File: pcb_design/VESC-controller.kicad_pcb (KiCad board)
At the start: 4 copper layers, 160 x 90 mm, 304 parts, among them J1 GATE_DRIVER_CONN_U, J2 GATE_DRIVER_CONN_V, J3 GATE_DRIVER_CONN_W, J4 micro USB, J5 ACCEL, J6 REGEN, J7 12V, J8 V_BUS, J9 SWD, P1 HALL/Encoder, P101 CANBUS, P2 Resolver, P3 PWR_COMM, Q1 BSC340N08, Q2 2N7002PW, Q3 AO4805, U1 STM32F40X_LQFP64, U10 LM2903-SO8, U11 LM3488, U12 OPA2376AID, U13 LM1117IMP-v.v, U14 OPA2376AID, U15 AD2S1205, U16 OPA2376AID, U17 LM2903-SO8, U18 AND3, U19 AD8397, U2 ISO1050, U20 APX809, U21 NCV78Mxx, U3 OPA2376AID, U4 LM2903-SO8, U5 7400-TSSOP, U6 SN74ALVC08PWR, U7 SN74ALVC08PWR, U8 SN74AUP1G74, U9 LM22676QTJ-5.0, X1 ABM3B - 8MHz, X2 ABM3B - 8MHz

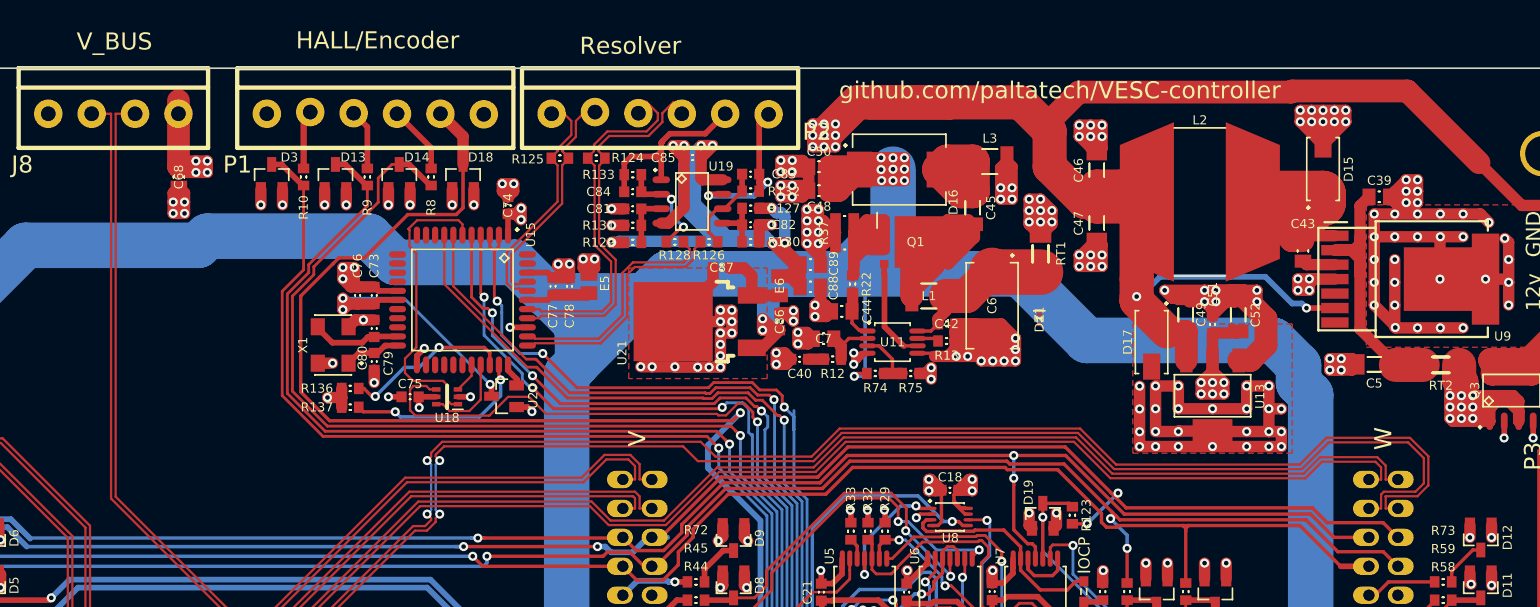
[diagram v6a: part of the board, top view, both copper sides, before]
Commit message: Had a missing pullup for the fault signal. Added silkcreens on the bottom
Signed-off-by: Marcos Chaparro <mchaparro@paltatech.com>
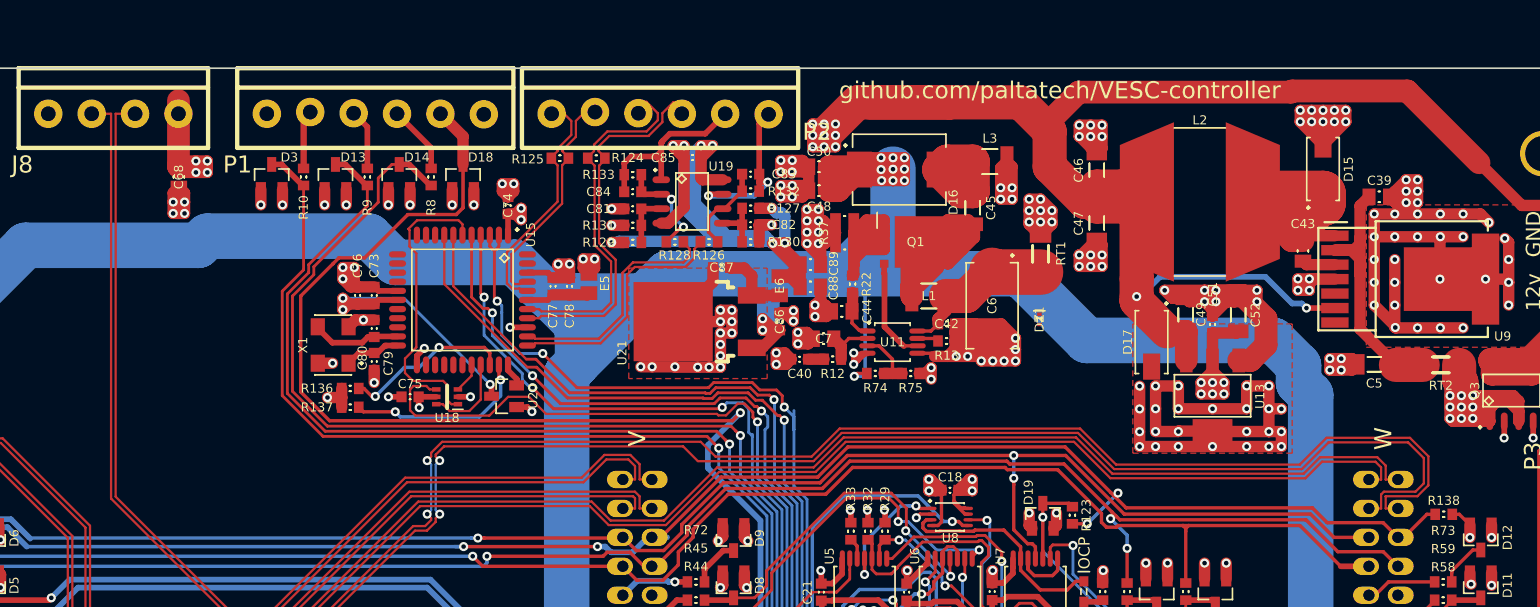
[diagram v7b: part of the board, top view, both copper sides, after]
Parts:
- added R138: 10k, IPC7351-Nominal:RESC1608X50, F.Cu at (63.8, -5.83)
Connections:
- net /MISO_RX_SCL renamed /STM32F4/MISO_ADC_EXT2
- net /RX_SCL_MOSI renamed /STM32F4/TX_SCL_MOSI
- net /SCK_ADC_EXT renamed /STM32F4/SCK_ADC_EXT
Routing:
- net ~FAULT: track 147.1 -> 151.2 mm
- net +3.3: track 192.5 -> 194.4 mm
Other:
- board text added: "+24v"
- board text added: "-VEE_CTRL"
- board text added: "3.3v"
- board text added: "5v"
- board text added: "9v-30v Supply"
- board text added: "ACCEL_IN"
- board text added: "ADC4/DAC1/RX PWM/I2C_SDA"
- board text added: "ADC5/DAC2 PWM/SPI1_SCK"
- board text added: "ADC6/PWM/ SPI1_MISO"
- board text added: "ADC7/TX PWM/I2C_SCL"
- board text added: "COS+"
- board text added: "COS-"
- board text added: "EXC+"
- board text added: "EXC-"
- board text added: "HALL_1"
- board text added: "HALL_2"
- board text added: "HALL_3"
- board text added: "I_phase+"
- board text added: "I_phase-"
- board text added: "PWM_BOT"
- board text added: "PWM_TOP"
- board text added: "PWR_GOOD"
- board text added: "REGEN_IN"
- board text added: "SIN+"
- board text added: "SIN-"
- board text added: "SUPPLY_SYNC"
- board text added: "TEMP"
- board text added: "VBUS(+)"
- board text added: "VBUS(-)"
- board text added: "V_phase+"
- board text added: "V_phase-"
- board text added: "~DRIVER_RESET"
- board text added: "~FAULT"

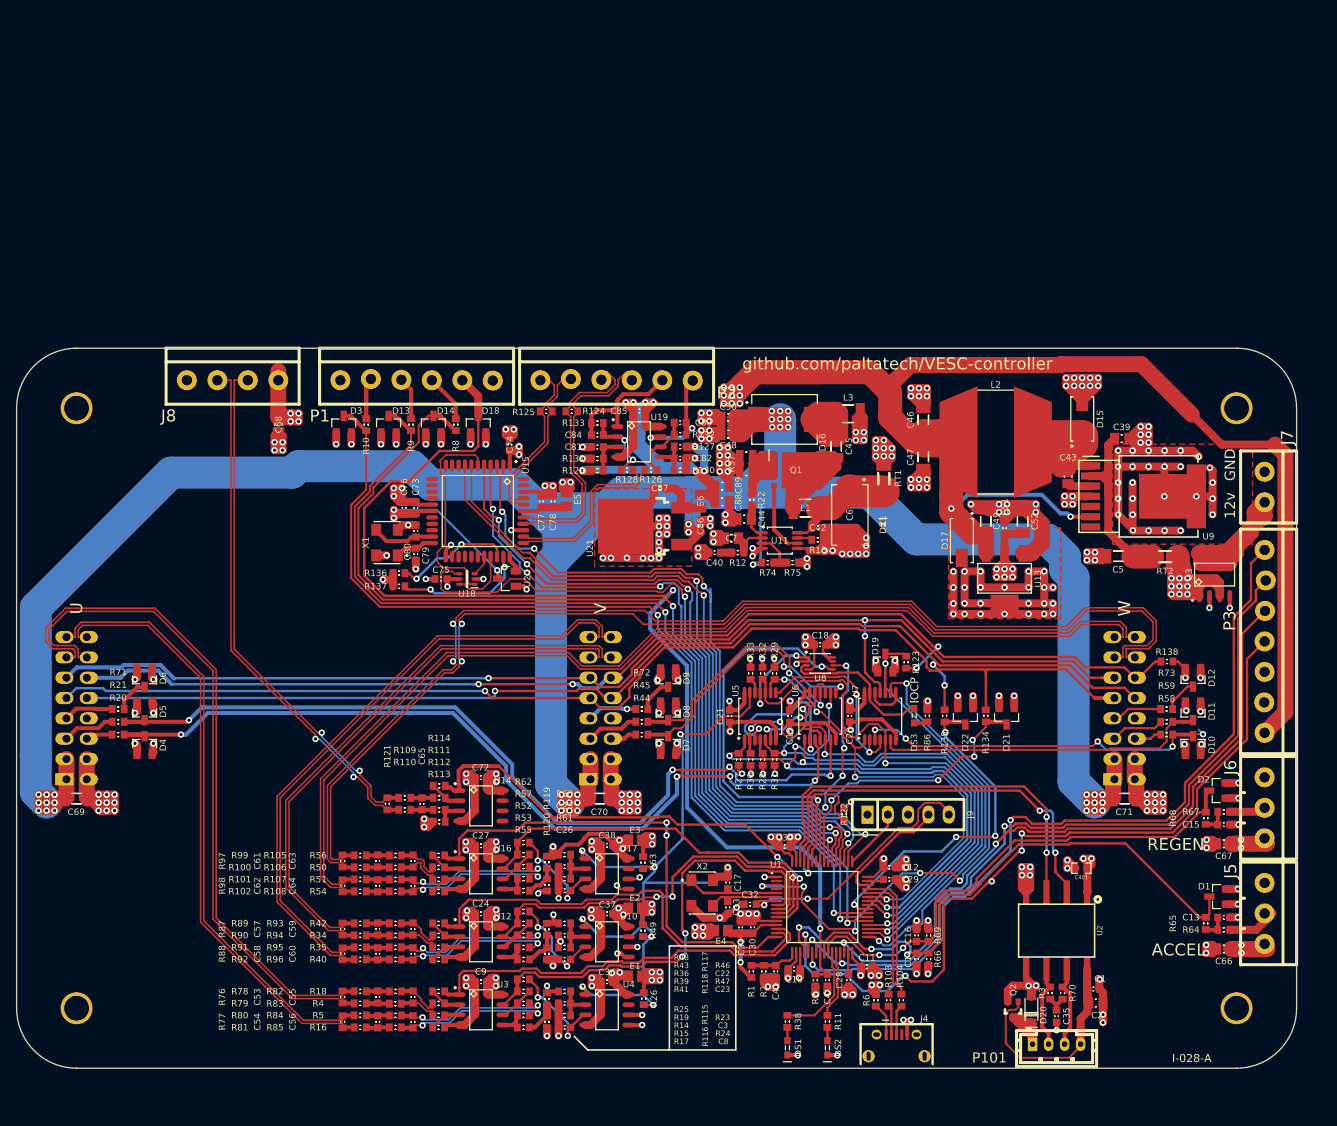
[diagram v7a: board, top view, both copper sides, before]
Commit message: Silkscreen logos, fixed swapped OCP inputs, added a button to enter bootloader,missing 3d model.
Signed-off-by: Marcos Chaparro <mchaparro@paltatech.com>
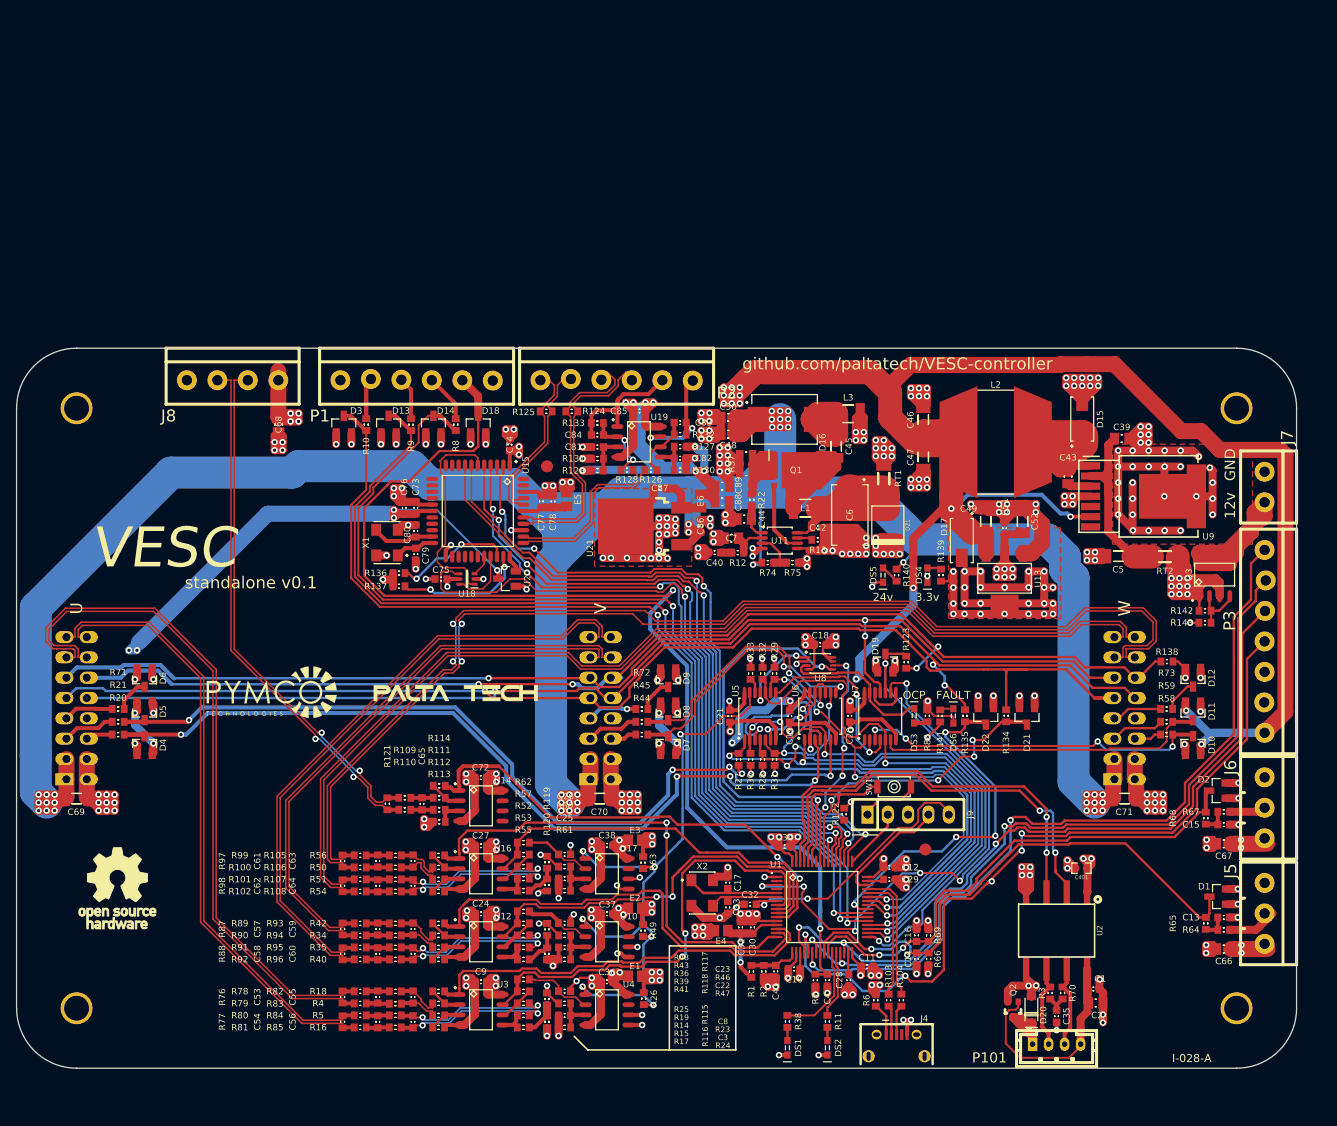
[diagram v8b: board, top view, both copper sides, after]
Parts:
- added DS4: GREEN, smd-semi:LED-0603, F.Cu at (33.8, -16.6)
- added DS5: RED, smd-semi:LED-0603, F.Cu at (28.3, -16.6)
- added DS6: FAULT, smd-semi:LED-0603, F.Cu at (37.1, 0.97)
- added G***: LOGO, paltatech:PYMCO_logo_22x15mm, F.Cu at (-48.2, -1.48)
- added G***: LOGO, mech:OSHW-10mm, F.Cu at (-67.4, 22.5)
- added G***: LOGO, paltatech:PALTA_TECH_SILKS_20mm, F.Cu at (-25.3, -1.88)
- added R139: 1k, IPC7351-Nominal:RESC1608X50, F.Cu at (35.5, -16.6)
- added R140: 10k, IPC7351-Nominal:RESC1608X50, F.Cu at (30.0, -16.6)
- added R141: 100R, IPC7351-Nominal:RESC1608X50, F.Cu at (35.4, 0.97)
- added R142: 10k, IPC7351-Nominal:RESC1608X50, F.Cu at (68.5, -12.2)
- added R143: 10k, IPC7351-Nominal:RESC1608X50, F.Cu at (68.5, -10.7)
- added REF**: FIDUCIAL-1.5mm, fab:FIDUCIAL-1.5mm, F.Cu at (-13.7, -30.2)
- added REF**: FIDUCIAL-1.5mm, fab:FIDUCIAL-1.5mm, F.Cu at (33.6, 17.7)
- added SW1: BOOTLOADER, paltatech:SMD-Switch_B3U-1000-B, F.Cu at (29.7, 9.82)
- DZ1: value ESD9L5.0ST5G -> 1SMB18CAT; footprint smd-semi:SOD-THAT -> w_smd_diode:do214aa
- U6, U7: value SN74ALVC08PWR -> SN74ACT08PWR
- moved C26 4.53 mm to (-11.5, 18.3), turned to 0 degrees
- moved C23 4.53 mm to (-11.5, 26.9), turned to 0 degrees
- moved C8 4.53 mm to (-11.5, 35.4), turned to 0 degrees
- moved R134 2.55 mm to (43.7, 0.95)
- moved D21 2.55 mm to (46.3, 0.95)
- moved D22 2.55 mm to (41.1, 0.95)
- moved R135 2.55 mm to (38.5, 0.95)
- moved C22 1.50 mm to (-11.5, 29.9)
- moved C25 1.50 mm to (-11.5, 21.3)
- moved C3 1.50 mm to (-11.5, 38.4)
- moved R23 1.50 mm to (-11.5, 36.9)
- moved R24 1.50 mm to (-11.5, 39.9)
- moved R46 1.50 mm to (-11.5, 28.4)
- moved R47 1.50 mm to (-11.5, 31.4)
- moved R60 1.50 mm to (-11.5, 19.8)
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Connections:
- C19 pad 2: +3.3 -> +5
- C20 pad 2: +3.3 -> +5
- D10 pad 2: +3.3 -> +5
- D11 pad 2: +3.3 -> +5
- D4 pad 2: +3.3 -> +5
- D5 pad 2: +3.3 -> +5
- D7 pad 2: +3.3 -> +5
- D8 pad 2: +3.3 -> +5
- Q3 pad 2: GND -> Net-(Q3-Pad2)
- Q3 pad 4: GND -> Net-(Q3-Pad2)
- U10 pad 2: Net-(C22-Pad1) -> Net-(C23-Pad1)
- U10 pad 3: Net-(C23-Pad1) -> Net-(C22-Pad1)
- U17 pad 2: Net-(C25-Pad1) -> Net-(C26-Pad1)
- U17 pad 3: Net-(C26-Pad1) -> Net-(C25-Pad1)
- U4 pad 2: Net-(C3-Pad1) -> Net-(C8-Pad1)
- U4 pad 3: Net-(C8-Pad1) -> Net-(C3-Pad1)
- U6 pad 14: +3.3 -> +5
- U7 pad 14: +3.3 -> +5
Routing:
- net +5: track 527.4 -> 682.2 mm, vias 28 -> 41
- net GND: track 700.5 -> 724.7 mm, vias 273 -> 286
- net Net-(C42-Pad1): track 14.1 -> 25.3 mm
- net /conditioning U/3.3V_AN: track 57.0 -> 48.8 mm
- net /conditioning U/OC_Fault: track 93.0 -> 84.9 mm
- net /conditioning W/3.3V_AN: track 46.4 -> 39.3 mm
- net Net-(Q3-Pad2): track 0.00 -> 6.78 mm
- net +24: track 406.2 -> 410.9 mm, vias 39 -> 40
- net Net-(C26-Pad1): track 12.8 -> 8.48 mm, vias 2 -> 0
- net Net-(C23-Pad1): track 12.7 -> 8.44 mm, vias 2 -> 0
- net Net-(C8-Pad1): track 13.1 -> 9.10 mm, vias 2 -> 0
- net Net-(R122-Pad1): track 17.8 -> 21.7 mm, vias 1 -> 0
- net /STM32F4/~FAULT: track 57.6 -> 61.4 mm, vias 2 -> 3
- net +3.3: track 194.4 -> 191.3 mm, vias 84 -> 76
- net /conditioning V/3.3V_AN: track 36.7 -> 39.5 mm
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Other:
- board text added: "24v"
- board text added: "CANH"
- board text added: "CANL"
- board text added: "FAULT"
- board text added: "VESC"
- board text added: "standalone v0.1"
